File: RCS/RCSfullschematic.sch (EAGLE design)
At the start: 76 parts, among them IC1 ILD213T, IC2 FT232RL, J2 MOTOR, J4 POWER, J5 SENSORS, J7 USB-MICROB, Q2 8 MHz, T1 2N2222, U1 MPL3115A2, U2 MPU-9250, U3 ATMEGA328P_TQFP, U4 ADS1015

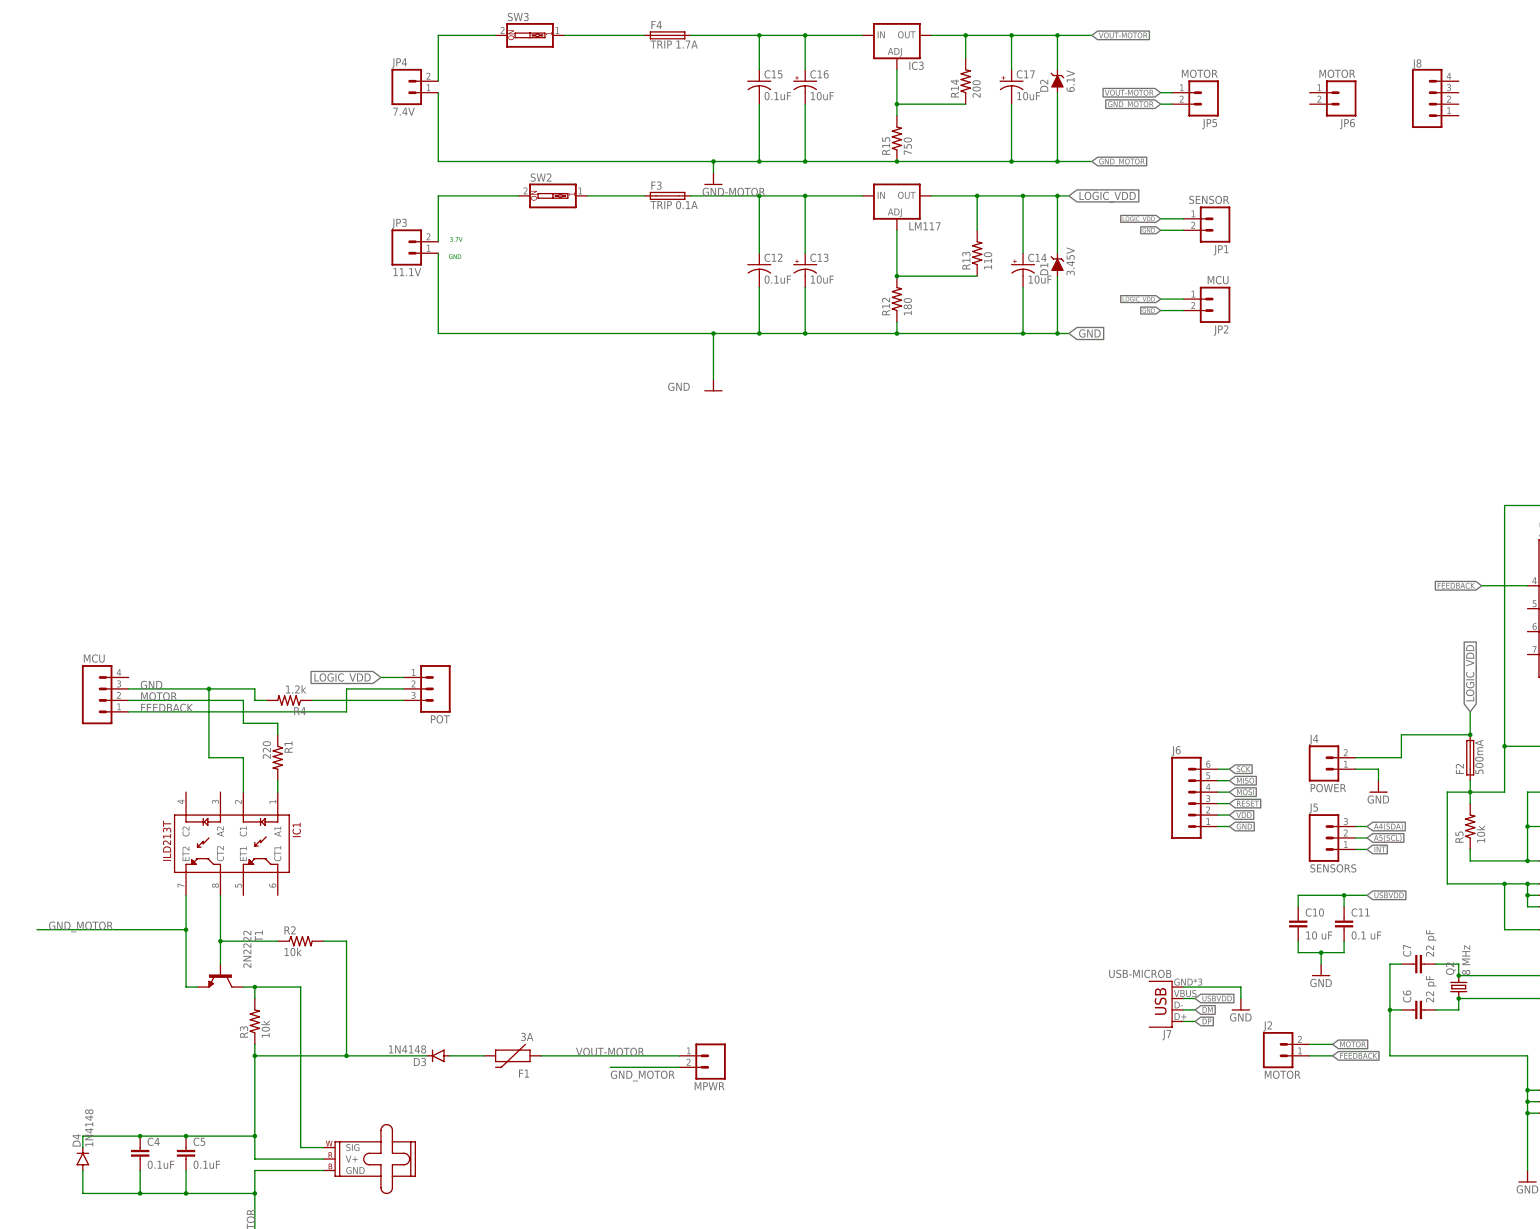
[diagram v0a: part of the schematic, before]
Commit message: Updated diode part
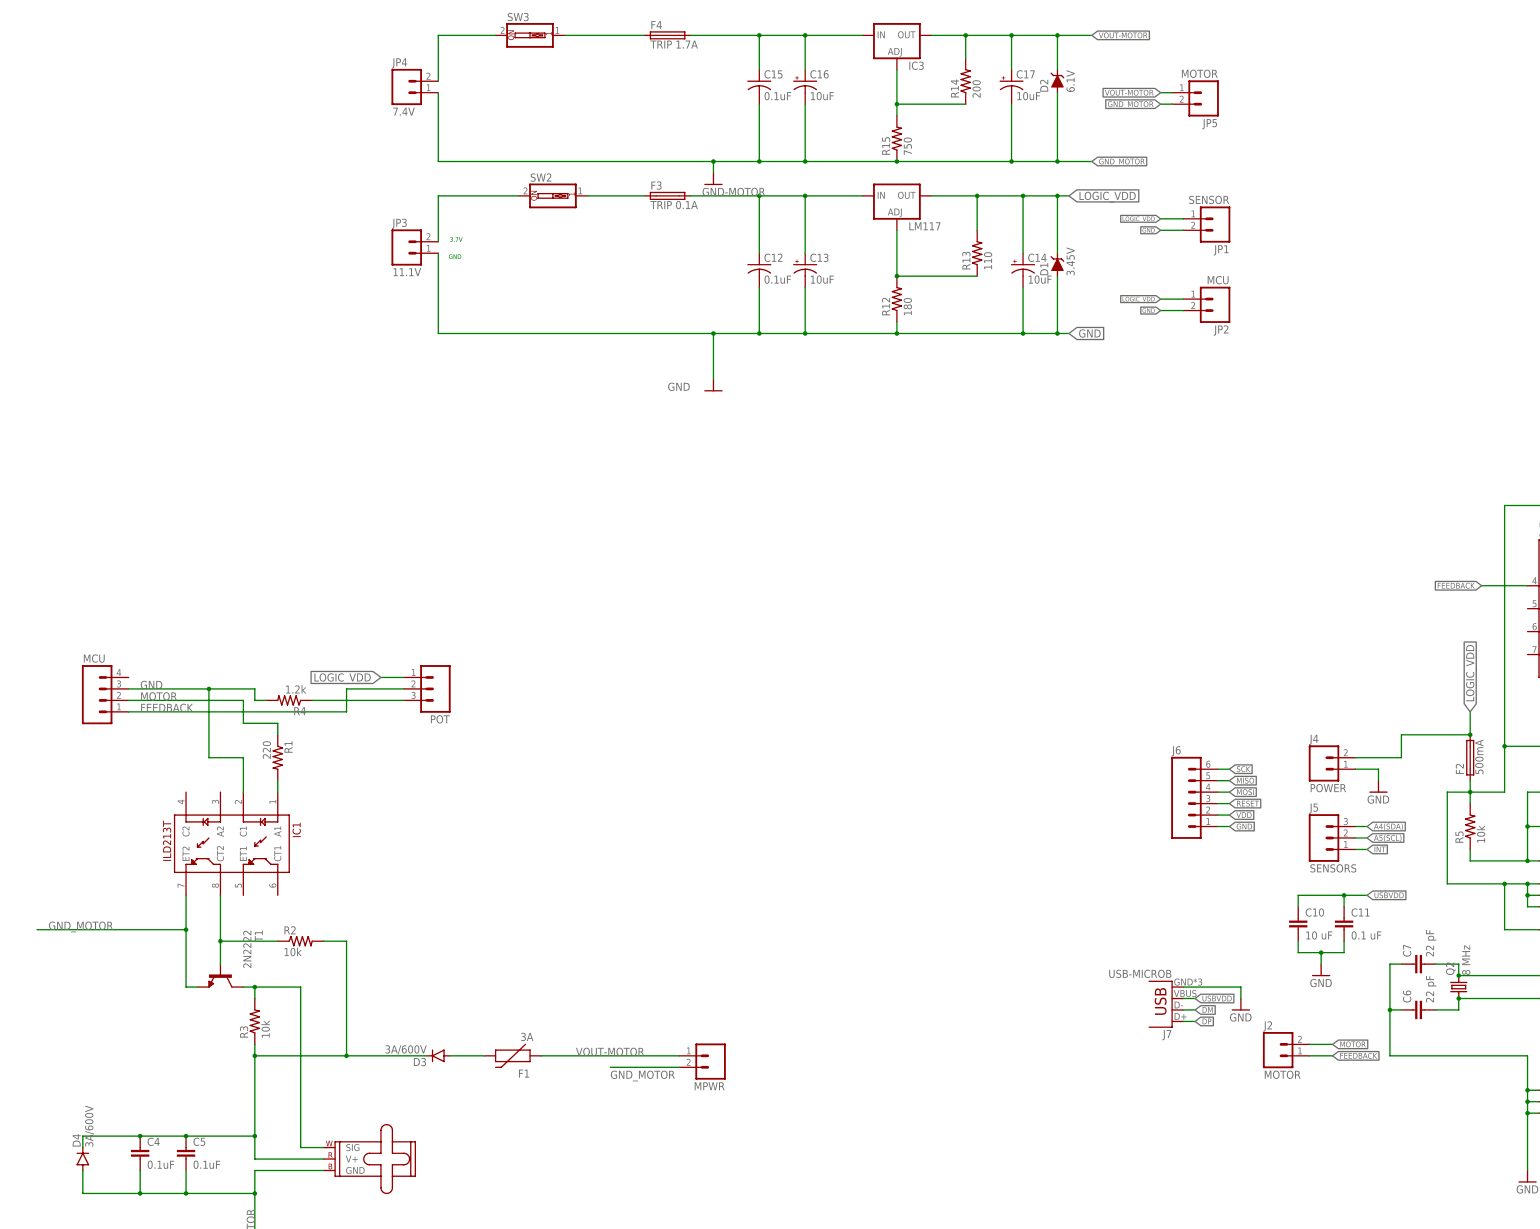
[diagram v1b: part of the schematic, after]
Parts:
- removed J8: (no value), SparkFun-Connectors:CONN_04
- removed JP6: MOTOR, SparkFun-Connectors:M02PTH
- D3, D4: value 1N4148 -> 3A/600V; device SparkFun-DiscreteSemi:DIODE1N4148 -> SparkFun-DiscreteSemi:DIODEES3J
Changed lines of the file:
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@@
 <?xml version="1.0" encoding="utf-8"?>
 <!DOCTYPE eagle SYSTEM "eagle.dtd">
-<eagle version="7.6.0">
+<eagle version="7.5.0">
 <drawing>
 <settings>
@@
 <part name="C4" library="SparkFun-Passives" deviceset="CAP" device="1206" value="0.1uF"/>
 <part name="C5" library="SparkFun-Passives" deviceset="CAP" device="1206" value="0.1uF"/>
-<part name="D3" library="SparkFun-DiscreteSemi" deviceset="DIODE" device="1N4148" value="1N4148"/>
-<part name="D4" library="SparkFun-DiscreteSemi" deviceset="DIODE" device="1N4148" value="1N4148"/>
+<part name="D3" library="SparkFun-DiscreteSemi" deviceset="DIODE" device="ES3J" value="3A/600V"/>
+<part name="D4" library="SparkFun-DiscreteSemi" deviceset="DIODE" device="ES3J" value="3A/600V"/>
 <part name="R1" library="SparkFun-Passives" deviceset="RESISTOR" device="1206" value="220"/>
 <part name="R2" library="SparkFun-Passives" deviceset="RESISTOR" device="1206" value="10k"/>
@@
 <part name="GND6" library="supply1" deviceset="GND" device="" value="GND-MOTOR"/>
 <part name="JP5" library="SparkFun-Connectors" deviceset="M02" device="PTH" value="MOTOR"/>
-<part name="JP6" library="SparkFun-Connectors" deviceset="M02" device="PTH" value="MOTOR"/>
-<part name="J8" library="SparkFun-Connectors" deviceset="CONN_04" device=""/>
 </parts>
 <sheets>
@@
 <instance part="GND6" gate="1" x="271.78" y="223.52"/>
 <instance part="JP5" gate="G$1" x="381" y="243.84" rot="R180"/>
-<instance part="JP6" gate="G$1" x="411.48" y="243.84" rot="R180"/>
-<instance part="J8" gate="G$1" x="431.8" y="241.3"/>
 </instances>
 <busses>

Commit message: updated parts
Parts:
- T1: value 2N2222 -> MMBT2222A; device adafruit:2N2222 -> SparkFun-DiscreteSemi:TRANSISTOR_NPNMMBT2222A
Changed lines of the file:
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@@
 <part name="R2" library="SparkFun-Passives" deviceset="RESISTOR" device="1206" value="10k"/>
 <part name="R3" library="SparkFun-Passives" deviceset="RESISTOR" device="1206" value="10k"/>
-<part name="T1" library="adafruit" deviceset="2N2222" device=""/>
+<part name="T1" library="SparkFun-DiscreteSemi" deviceset="TRANSISTOR_NPN" device="MMBT2222A" value="MMBT2222A"/>
 <part name="IC1" library="SparkFun-DiscreteSemi" deviceset="ILD213T" device=""/>
 <part name="MPWR" library="SparkFun-Connectors" deviceset="M02" device="PTH"/>
